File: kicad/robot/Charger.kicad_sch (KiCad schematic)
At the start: 32 parts, among them SW1 76EXTSM, U13 MAX77976EFD+

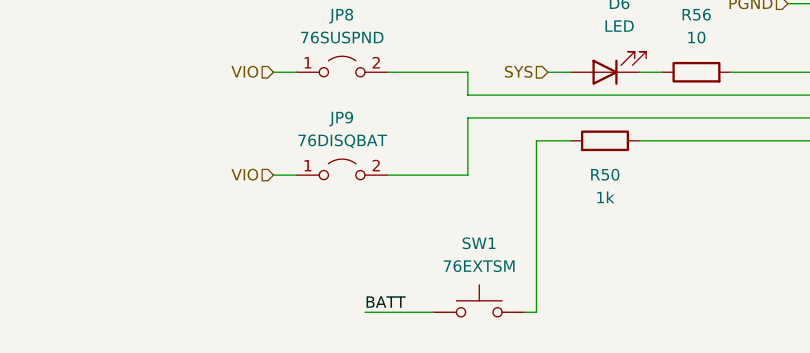
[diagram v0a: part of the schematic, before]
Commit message: Replaced push switch with 2-pad shorting TP
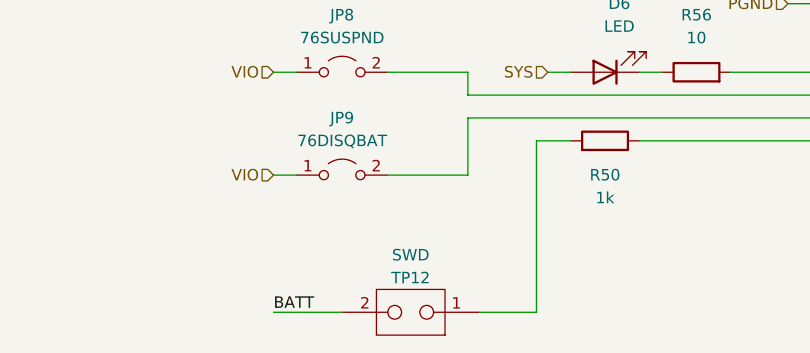
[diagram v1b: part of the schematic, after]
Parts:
- removed SW1: 76EXTSM, symbol Switch:SW_Push
- added TP12: SWD, TestPoint:TestPoint_2Pads_Pitch2mm_SMD, symbol custom_connectors:TestPoint_CurrentShunt
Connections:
- net BATT: now also TP12.2
- net at R50.2: now also TP12.1
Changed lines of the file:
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@@
     (stroke (width 0) (type default) (color 0 0 0 0))
   )
-  (wire (pts (xy 45.72 163.83) (xy 53.34 163.83))
+  (wire (pts (xy 35.56 163.83) (xy 43.18 163.83))
     (stroke (width 0) (type default) (color 0 0 0 0))
   )
@@
     (stroke (width 0) (type default) (color 0 0 0 0))
   )
-  (wire (pts (xy 63.5 163.83) (xy 64.77 163.83))
+  (wire (pts (xy 58.42 163.83) (xy 64.77 163.83))
     (stroke (width 0) (type default) (color 0 0 0 0))
   )
@@
     (effects (font (size 1.27 1.27)) (justify left bottom))
   )
-  (label "BATT" (at 45.72 163.83 0)
+  (label "BATT" (at 35.56 163.83 0)
     (effects (font (size 1.27 1.27)) (justify left bottom))
   )
@@
     )
     (property "Description" "16V 1210 100uF" (id 4) (at 255.27 105.41 0))
+    (pin "1")
+    (pin "2")
+  )
+  (symbol (lib_id "custom_connectors:TestPoint_CurrentShunt") (at 50.8 163.83 180) (unit 1)
+    (in_bom no) (on_board yes)
+    (property "Reference" "TP12" (id 0) (at 50.8 160.02 0))
+    (property "Value" "SWD" (id 1) (at 50.8 157.48 0))
+    (property "Footprint" "TestPoint:TestPoint_2Pads_Pitch2mm_SMD" (id 2) (at 50.8 168.91 0)
+      (effects (font (size 1.27 1.27)) hide)
+    )
+    (property "Datasheet" "https://www.digikey.jp/product-detail/en/kycon-inc/SX1100-B/2092-SX1100-B-ND/9990206" (id 3) (at 50.8 171.45 0)
+      (effects (font (size 1.27 1.27)) hide)
+    )
     (pin "1")
     (pin "2")
@@
     (pin "1")
     (pin "2")
-  )
-  (symbol (lib_id "Switch:SW_Push") (at 58.42 163.83 0) (unit 1)
-    (in_bom yes) (on_board yes) (fields_autoplaced)
-    (property "Reference" "SW1" (id 0) (at 58.42 156.21 0))
-    (property "Value" "76EXTSM" (id 1) (at 58.42 158.75 0))
-    (property "Footprint" "" (id 2) (at 58.42 158.75 0)
-      (effects (font (size 1.27 1.27)) hide)
-    )
-    (property "Datasheet" "~" (id 3) (at 58.42 158.75 0)
-      (effects (font (size 1.27 1.27)) hide)
-    )
-    (pin "1")
-    (pin "2")

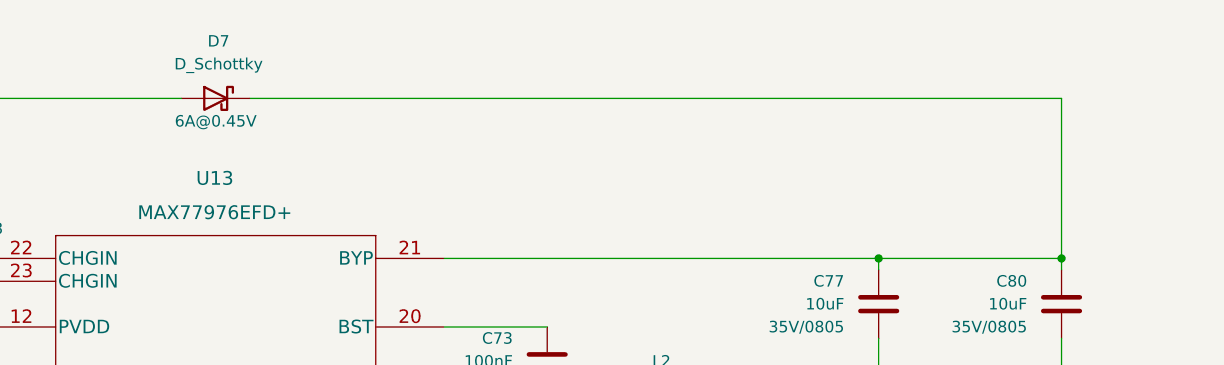
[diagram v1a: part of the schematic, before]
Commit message: added SS1P3L-M3_84A diode to charger
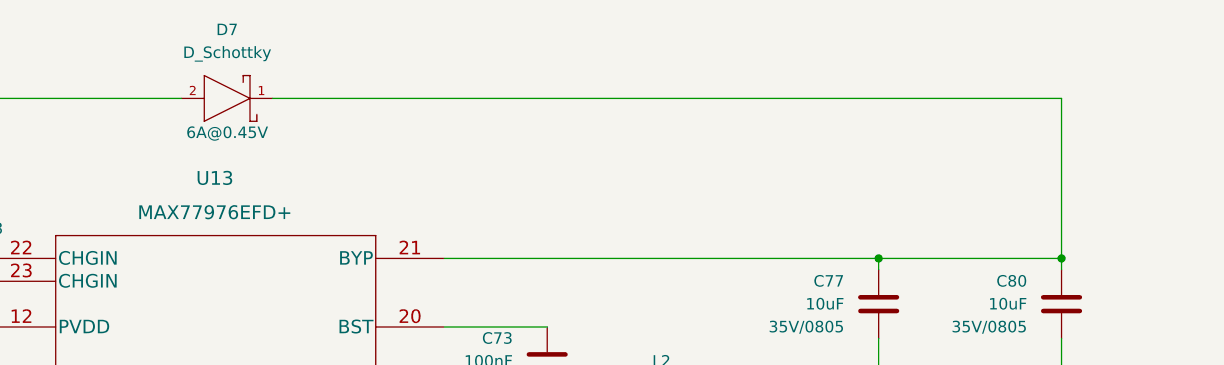
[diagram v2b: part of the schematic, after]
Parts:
- D7: footprint (none) -> Diode_SMD:Vishay-SS1P3L-M3_84A-0-0-0; symbol Device:D_Schottky -> Diode:SS1P3L-M3_84A; category (none) -> Diode; device class L1 (none) -> Discrete Semiconductors; device class L2 (none) -> Diodes; device class L3 (none) -> Schottky Diodes; digikey description (none) -> DIODE SCHOTTKY 30V 1.5A DO220AA; digikey part number (none) -> SS1P3L-M3/84AGICT-ND; forward current (none) -> 1A; height (none) -> 1.15mm; lead free (none) -> yes; library id (none) -> e43f9aab7730c7ed; manufacturer (none) -> Vishay; max junction temp (none) -> +150°C; max repetitive reverse voltage (none) -> 30V; max surge forward current (none) -> 50A; mouser description (none) -> Schottky Diodes & Rectifiers 30volt 1.0amp; mouser part number (none) -> 625-SS1P3L-M3/84A; package (none) -> DO-220AA; peak reverse current (none) -> 200uA; reverse voltage (none) -> 30V; rohs (none) -> yes; temperature range high (none) -> +150°C; temperature range low (none) -> -55°C
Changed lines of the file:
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@@
+    (stroke (width 0) (type default) (color 0 0 0 0))
+  )
+  (wire (pts (xy 128.27 63.5) (xy 215.9 63.5))
     (stroke (width 0) (type default) (color 0 0 0 0))
   )
@@
   )
   (wire (pts (xy 53.34 104.14) (xy 58.42 104.14))
-    (stroke (width 0) (type default) (color 0 0 0 0))
-  )
-  (wire (pts (xy 125.73 63.5) (xy 215.9 63.5))
     (stroke (width 0) (type default) (color 0 0 0 0))
   )
@@
     (pin "2")
   )
-  (symbol (lib_id "Device:D_Schottky") (at 121.92 63.5 0) (mirror y) (unit 1)
-    (in_bom yes) (on_board yes)
-    (property "Reference" "D7" (id 0) (at 122.2375 57.15 0))
-    (property "Value" "D_Schottky" (id 1) (at 122.2375 59.69 0))
-    (property "Footprint" "" (id 2) (at 121.92 63.5 0)
-      (effects (font (size 1.27 1.27)) hide)
-    )
-    (property "Datasheet" "~" (id 3) (at 121.92 63.5 0)
-      (effects (font (size 1.27 1.27)) hide)
-    )
-    (property "Description" "6A@0.45V" (id 4) (at 121.92 66.04 0))
-    (pin "1")
-    (pin "2")
+  (symbol (lib_id "Diode:SS1P3L-M3_84A") (at 115.57 63.5 0) (unit 1)
+    (in_bom yes) (on_board yes)
+    (property "Reference" "D7" (id 0) (at 123.19 55.88 0))
+    (property "Value" "D_Schottky" (id 1) (at 123.19 58.42 0))
+    (property "Footprint" "Diode_SMD:Vishay-SS1P3L-M3_84A-0-0-0" (id 2) (at 115.57 53.34 0)
+      (effects (font (size 1.27 1.27)) (justify left) hide)
+    )
+    (property "Datasheet" "https://www.vishay.com/docs/88915/ss1p3l.pdf" (id 3) (at 115.57 50.8 0)
+      (effects (font (size 1.27 1.27)) (justify left) hide)
+    )
+    (property "Description" "6A@0.45V" (id 4) (at 123.19 67.31 0))
+    (property "category" "Diode" (id 5) (at 115.57 48.26 0)
+      (effects (font (size 1.27 1.27)) (justify left) hide)
+    )
+    (property "device class L1" "Discrete Semiconductors" (id 6) (at 115.57 45.72 0)
+      (effects (font (size 1.27 1.27)) (justify left) hide)
+    )
+    (property "device class L2" "Diodes" (id 7) (at 115.57 43.18 0)
+      (effects (font (size 1.27 1.27)) (justify left) hide)
+    )
+    (property "device class L3" "Schottky Diodes" (id 8) (at 115.57 40.64 0)
+      (effects (font (size 1.27 1.27)) (justify left) hide)
+    )
+    (property "digikey description" "DIODE SCHOTTKY 30V 1.5A DO220AA" (id 9) (at 115.57 38.1 0)
+      (effects (font (size 1.27 1.27)) (justify left) hide)
+    )
+    (property "digikey part number" "SS1P3L-M3/84AGICT-ND" (id 10) (at 115.57 35.56 0)
+      (effects (font (size 1.27 1.27)) (justify left) hide)
+    )
+    (property "forward current" "1A" (id 11) (at 115.57 33.02 0)
+      (effects (font (size 1.27 1.27)) (justify left) hide)
+    )
+    (property "height" "1.15mm" (id 12) (at 115.57 30.48 0)
+      (effects (font (size 1.27 1.27)) (justify left) hide)
+    )
+    (property "lead free" "yes" (id 13) (at 115.57 27.94 0)
+      (effects (font (size 1.27 1.27)) (justify left) hide)
+    )
+    (property "library id" "e43f9aab7730c7ed" (id 14) (at 115.57 25.4 0)
+      (effects (font (size 1.27 1.27)) (justify left) hide)
+    )
+    (property "manufacturer" "Vishay" (id 15) (at 115.57 22.86 0)
+      (effects (font (size 1.27 1.27)) (justify left) hide)
+    )
+    (property "max junction temp" "+150°C" (id 16) (at 115.57 20.32 0)
+      (effects (font (size 1.27 1.27)) (justify left) hide)
+    )
+    (property "max repetitive reverse voltage" "30V" (id 17) (at 115.57 17.78 0)
+      (effects (font (size 1.27 1.27)) (justify left) hide)
+    )
+    (property "max surge forward current" "50A" (id 18) (at 115.57 15.24 0)
+      (effects (font (size 1.27 1.27)) (justify left) hide)
+    )
+    (property "mouser description" "Schottky Diodes & Rectifiers 30volt 1.0amp" (id 19) (at 115.57 12.7 0)
+      (effects (font (size 1.27 1.27)) (justify left) hide)
+    )
+    (property "mouser part number" "625-SS1P3L-M3/84A" (id 20) (at 115.57 10.16 0)
+      (effects (font (size 1.27 1.27)) (justify left) hide)
+    )
+    (property "package" "DO-220AA" (id 21) (at 115.57 7.62 0)
+      (effects (font (size 1.27 1.27)) (justify left) hide)
+    )
+    (property "peak reverse current" "200uA" (id 22) (at 115.57 5.08 0)
+      (effects (font (size 1.27 1.27)) (justify left) hide)
+    )
+    (property "reverse voltage" "30V" (id 23) (at 115.57 2.54 0)
+      (effects (font (size 1.27 1.27)) (justify left) hide)
+    )
+    (property "rohs" "yes" (id 24) (at 115.57 0 0)
+      (effects (font (size 1.27 1.27)) (justify left) hide)
+    )
+    (property "temperature range high" "+150°C" (id 25) (at 115.57 -2.54 0)
+      (effects (font (size 1.27 1.27)) (justify left) hide)
+    )
+    (property "temperature range low" "-55°C" (id 26) (at 115.57 -5.08 0)
+      (effects (font (size 1.27 1.27)) (justify left) hide)
+    )
+    (pin "1")
+    (pin "2")

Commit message: Updated footprint for all closed jumpers
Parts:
- JP7: footprint custom_connectors:2.54mm_2pointCurrentTestPoint -> custom_connectors:2.54mm_2pointJumperClosed
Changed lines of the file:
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@@
     (property "Reference" "JP7" (id 0) (at 33.02 102.87 0))
     (property "Value" "76VIO" (id 1) (at 33.02 105.41 0))
-    (property "Footprint" "custom_connectors:2.54mm_2pointCurrentTestPoint" (id 2) (at 33.02 109.22 0)
+    (property "Footprint" "custom_connectors:2.54mm_2pointJumperClosed" (id 2) (at 33.02 109.22 0)
       (effects (font (size 1.27 1.27)) hide)
     )

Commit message: Added footprint for all open jumper to schamtic and pcb
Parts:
- JP8, JP9: footprint custom_connectors:2.54mm_2pointCurrentTestPoint -> custom_connectors:2.54mm_2pointJumperOpen
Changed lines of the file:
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@@
     (pin "2")
   )
-  (symbol (lib_id "Jumper:Jumper_2_Open") (at 43.18 137.16 0) (unit 1)
+  (symbol (lib_name "Jumper_2_Open_1") (lib_id "Jumper:Jumper_2_Open") (at 43.18 137.16 0) (unit 1)
     (in_bom yes) (on_board yes) (fields_autoplaced)
     (property "Reference" "JP8" (id 0) (at 43.18 130.81 0))
     (property "Value" "76SUSPND" (id 1) (at 43.18 133.35 0))
-    (property "Footprint" "custom_connectors:2.54mm_2pointCurrentTestPoint" (id 2) (at 43.18 137.16 0)
+    (property "Footprint" "custom_connectors:2.54mm_2pointJumperOpen" (id 2) (at 43.18 137.16 0)
       (effects (font (size 1.27 1.27)) hide)
     )
@@
     (property "Reference" "JP9" (id 0) (at 43.18 142.24 0))
     (property "Value" "76DISQBAT" (id 1) (at 43.18 144.78 0))
-    (property "Footprint" "custom_connectors:2.54mm_2pointCurrentTestPoint" (id 2) (at 43.18 148.59 0)
+    (property "Footprint" "custom_connectors:2.54mm_2pointJumperOpen" (id 2) (at 43.18 148.59 0)
       (effects (font (size 1.27 1.27)) hide)
     )

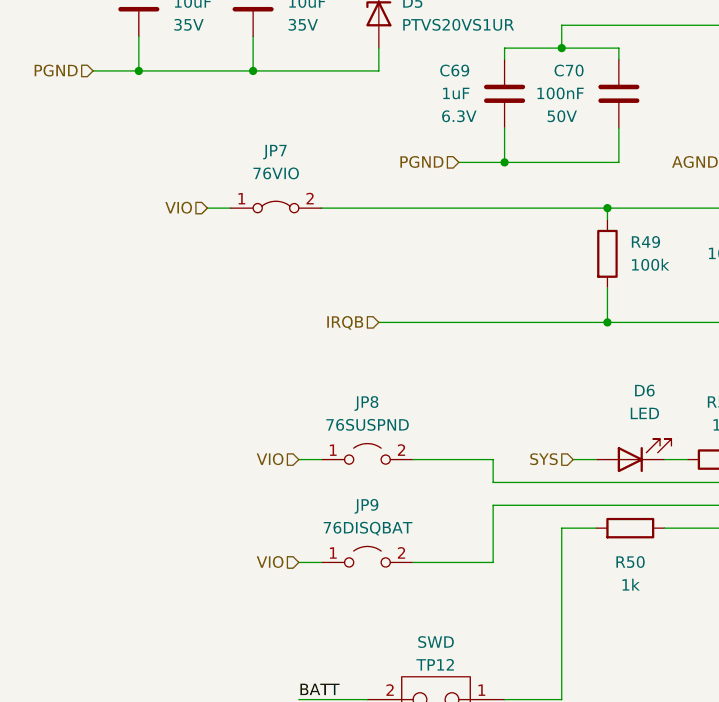
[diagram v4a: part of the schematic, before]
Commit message: Updated values for all jumpers to organize BOM
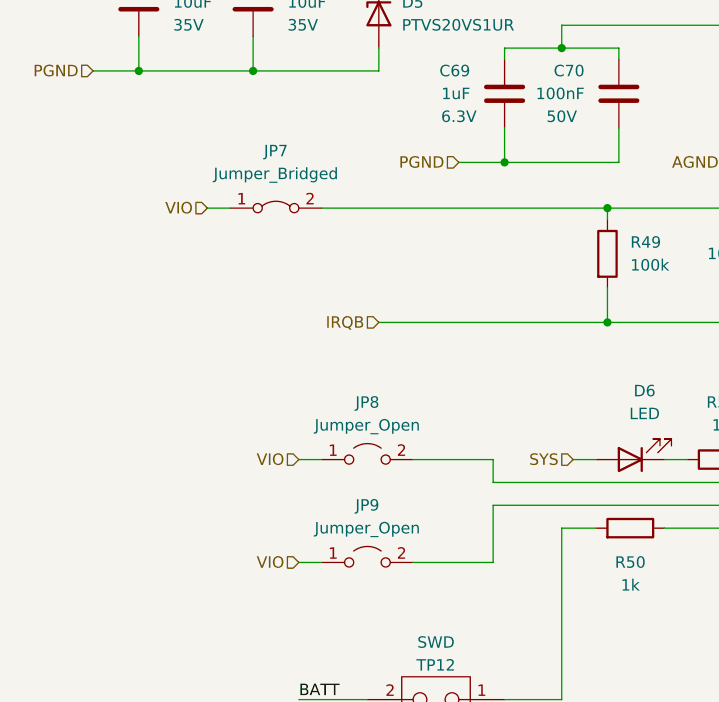
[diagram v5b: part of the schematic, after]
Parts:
- JP7: value 76VIO -> Jumper_Bridged
- JP8: value 76SUSPND -> Jumper_Open
- JP9: value 76DISQBAT -> Jumper_Open
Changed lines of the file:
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@@
     (in_bom yes) (on_board yes) (fields_autoplaced)
     (property "Reference" "JP8" (id 0) (at 43.18 130.81 0))
-    (property "Value" "76SUSPND" (id 1) (at 43.18 133.35 0))
+    (property "Value" "Jumper_Open" (id 1) (at 43.18 133.35 0))
     (property "Footprint" "custom_connectors:2.54mm_2pointJumperOpen" (id 2) (at 43.18 137.16 0)
       (effects (font (size 1.27 1.27)) hide)
@@
     (in_bom yes) (on_board yes) (fields_autoplaced)
     (property "Reference" "JP9" (id 0) (at 43.18 142.24 0))
-    (property "Value" "76DISQBAT" (id 1) (at 43.18 144.78 0))
+    (property "Value" "Jumper_Open" (id 1) (at 43.18 144.78 0))
     (property "Footprint" "custom_connectors:2.54mm_2pointJumperOpen" (id 2) (at 43.18 148.59 0)
       (effects (font (size 1.27 1.27)) hide)
@@
   )
   (symbol (lib_id "Jumper:Jumper_2_Bridged") (at 33.02 109.22 0) (unit 1)
-    (in_bom yes) (on_board yes) (fields_autoplaced)
+    (in_bom yes) (on_board yes)
     (property "Reference" "JP7" (id 0) (at 33.02 102.87 0))
-    (property "Value" "76VIO" (id 1) (at 33.02 105.41 0))
+    (property "Value" "Jumper_Bridged" (id 1) (at 33.02 105.41 0))
     (property "Footprint" "custom_connectors:2.54mm_2pointJumperClosed" (id 2) (at 33.02 109.22 0)
       (effects (font (size 1.27 1.27)) hide)

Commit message: WARNING Major BOM cleanup
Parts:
- D6: value LED -> LED_YG
- TP12: value SWD -> TP2PinPads
- TP23, TP24, TP25, TP26: value TestPoint -> TP5002
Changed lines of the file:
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@@
     (in_bom no) (on_board yes)
     (property "Reference" "TP12" (id 0) (at 50.8 160.02 0))
-    (property "Value" "SWD" (id 1) (at 50.8 157.48 0))
+    (property "Value" "TP2PinPads" (id 1) (at 50.8 157.48 0))
     (property "Footprint" "TestPoint:TestPoint_2Pads_Pitch2mm_SMD" (id 2) (at 50.8 168.91 0)
       (effects (font (size 1.27 1.27)) hide)
     )
     (property "Datasheet" "https://www.digikey.jp/product-detail/en/kycon-inc/SX1100-B/2092-SX1100-B-ND/9990206" (id 3) (at 50.8 171.45 0)
+      (effects (font (size 1.27 1.27)) hide)
+    )
+    (property "Description" "ExtSM" (id 4) (at 50.8 163.83 0)
       (effects (font (size 1.27 1.27)) hide)
     )
@@
       (effects (font (size 1.27 1.27)) (justify left))
     )
-    (property "Value" "TestPoint" (id 1) (at 194.31 122.4279 0)
+    (property "Value" "TP5002" (id 1) (at 194.31 122.4279 0)
       (effects (font (size 1.27 1.27)) (justify left) hide)
     )
@@
     )
     (property "Datasheet" "~" (id 3) (at 196.85 124.46 0)
+      (effects (font (size 1.27 1.27)) hide)
+    )
+    (property "Description" "BATT" (id 4) (at 191.77 124.46 0)
       (effects (font (size 1.27 1.27)) hide)
     )
@@
       (effects (font (size 1.27 1.27)) (justify left))
     )
-    (property "Value" "TestPoint" (id 1) (at 270.51 97.0279 0)
+    (property "Value" "TP5002" (id 1) (at 270.51 97.0279 0)
       (effects (font (size 1.27 1.27)) (justify left) hide)
     )
@@
     )
     (property "Datasheet" "~" (id 3) (at 273.05 99.06 0)
+      (effects (font (size 1.27 1.27)) hide)
+    )
+    (property "Description" "SYS" (id 4) (at 267.97 99.06 0)
       (effects (font (size 1.27 1.27)) hide)
     )
@@
     (in_bom yes) (on_board yes) (fields_autoplaced)
     (property "Reference" "D6" (id 0) (at 73.9775 129.54 0))
-    (property "Value" "LED" (id 1) (at 73.9775 132.08 0))
+    (property "Value" "LED_YG" (id 1) (at 73.9775 132.08 0))
     (property "Footprint" "Diode_SMD:D_0603_1608Metric_Harvatek" (id 2) (at 72.39 137.16 0)
       (effects (font (size 1.27 1.27)) hide)
@@
       (effects (font (size 1.27 1.27)) (justify left))
     )
-    (property "Value" "TestPoint" (id 1) (at 93.98 79.2479 0)
+    (property "Value" "TP5002" (id 1) (at 93.98 79.2479 0)
       (effects (font (size 1.27 1.27)) (justify left) hide)
     )
@@
     )
     (property "Datasheet" "~" (id 3) (at 96.52 81.28 0)
+      (effects (font (size 1.27 1.27)) hide)
+    )
+    (property "Description" "CHGIN" (id 4) (at 91.44 81.28 0)
       (effects (font (size 1.27 1.27)) hide)
     )
@@
       (effects (font (size 1.27 1.27)) (justify right))
     )
-    (property "Value" "TestPoint" (id 1) (at 270.51 111.2521 0)
+    (property "Value" "TP5002" (id 1) (at 270.51 111.2521 0)
       (effects (font (size 1.27 1.27)) (justify left) hide)
     )
@@
       (effects (font (size 1.27 1.27)) hide)
     )
+    (property "Description" "PGND" (id 4) (at 267.97 109.22 0)
+      (effects (font (size 1.27 1.27)) hide)
+    )

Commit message: WARNING more BOM batch edits
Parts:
- TP12: Part Number (none) -> N/A
- TP23, TP24, TP25, TP26: Manufacturer (none) -> Keystone Electronics; Part Number (none) -> 5002
- U13: Part Number (none) -> MAX77976EFD+
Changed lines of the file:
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@@
+      (effects (font (size 1.27 1.27)) hide)
+    )
+    (property "Part Number" "N/A" (id 5) (at 50.8 163.83 0)
       (effects (font (size 1.27 1.27)) hide)
     )
@@
     )
     (property "Description" "BATT" (id 4) (at 191.77 124.46 0)
+      (effects (font (size 1.27 1.27)) hide)
+    )
+    (property "Manufacturer" "Keystone Electronics" (id 5) (at 191.77 124.46 0)
+      (effects (font (size 1.27 1.27)) hide)
+    )
+    (property "Part Number" "5002" (id 6) (at 191.77 124.46 0)
       (effects (font (size 1.27 1.27)) hide)
     )
@@
       (effects (font (size 1.27 1.27)) hide)
     )
+    (property "Manufacturer" "Keystone Electronics" (id 5) (at 267.97 99.06 0)
+      (effects (font (size 1.27 1.27)) hide)
+    )
+    (property "Part Number" "5002" (id 6) (at 267.97 99.06 0)
+      (effects (font (size 1.27 1.27)) hide)
+    )
     (pin "1")
   )
@@
     )
     (property "Description" "Current limit > 9.5A" (id 4) (at 121.92 106.68 0)
+      (effects (font (size 1.27 1.27)) hide)
+    )
+    (property "Part Number" "MAX77976EFD+" (id 5) (at 121.92 106.68 0)
       (effects (font (size 1.27 1.27)) hide)
     )
@@
       (effects (font (size 1.27 1.27)) hide)
     )
+    (property "Manufacturer" "Keystone Electronics" (id 5) (at 91.44 81.28 0)
+      (effects (font (size 1.27 1.27)) hide)
+    )
+    (property "Part Number" "5002" (id 6) (at 91.44 81.28 0)
+      (effects (font (size 1.27 1.27)) hide)
+    )
     (pin "1")
   )
@@
       (effects (font (size 1.27 1.27)) hide)
     )
+    (property "Manufacturer" "Keystone Electronics" (id 5) (at 267.97 109.22 0)
+      (effects (font (size 1.27 1.27)) hide)
+    )
+    (property "Part Number" "5002" (id 6) (at 267.97 109.22 0)
+      (effects (font (size 1.27 1.27)) hide)
+    )
